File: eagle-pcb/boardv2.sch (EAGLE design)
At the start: 11 parts, among them IC1 ATTINY85, J1 FEMALE 2x3, X1 USBPCB

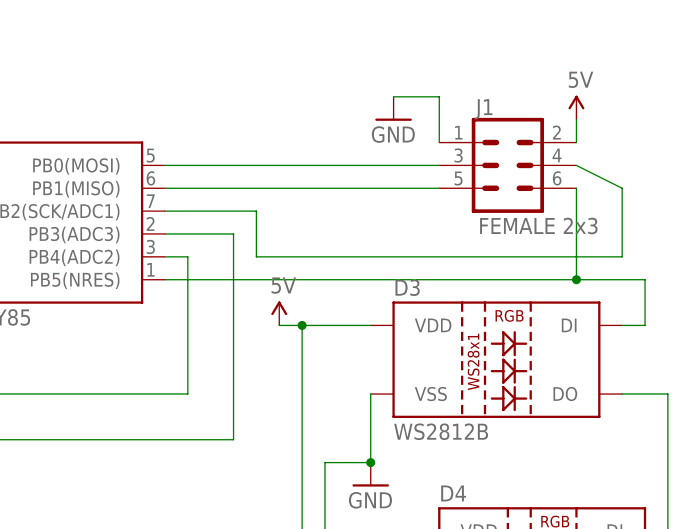
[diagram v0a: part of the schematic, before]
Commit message: FIX pcb, use MOSI to drive LED, not RESET
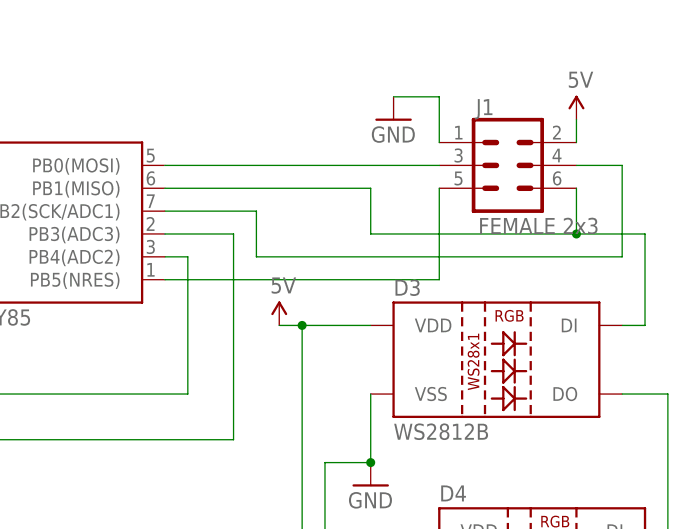
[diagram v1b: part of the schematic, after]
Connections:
- removed net RESET/LED: D3.DI, IC1.PB5(NRES), J1.6
- new net RESET: IC1.PB5(NRES), J1.5
- net MISO: now also D3.DI, J1.6; no longer J1.5
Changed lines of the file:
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@@
 <?xml version="1.0" encoding="utf-8"?>
 <!DOCTYPE eagle SYSTEM "eagle.dtd">
-<eagle version="9.6.1">
+<eagle version="9.6.2">
 <drawing>
 <settings>
@@
 </segment>
 </net>
-<net name="RESET/LED" class="0">
-<segment>
-<pinref part="D3" gate="G$1" pin="DI"/>
-<wire x1="127" y1="27.94" x2="124.46" y2="27.94" width="0.1524" layer="91"/>
-<wire x1="127" y1="33.02" x2="127" y2="27.94" width="0.1524" layer="91"/>
+<net name="RESET" class="0">
+<segment>
 <pinref part="IC1" gate="G$1" pin="PB5(NRES)"/>
-<wire x1="73.66" y1="33.02" x2="119.38" y2="33.02" width="0.1524" layer="91"/>
-<pinref part="J1" gate="G$1" pin="6"/>
-<wire x1="119.38" y1="33.02" x2="127" y2="33.02" width="0.1524" layer="91"/>
-<wire x1="119.38" y1="43.18" x2="119.38" y2="33.02" width="0.1524" layer="91"/>
-<junction x="119.38" y="33.02"/>
+<wire x1="73.66" y1="33.02" x2="104.14" y2="33.02" width="0.1524" layer="91"/>
+<pinref part="J1" gate="G$1" pin="5"/>
+<wire x1="104.14" y1="43.18" x2="104.14" y2="33.02" width="0.1524" layer="91"/>
 </segment>
 </net>
@@
 <wire x1="83.82" y1="35.56" x2="124.46" y2="35.56" width="0.1524" layer="91"/>
 <pinref part="J1" gate="G$1" pin="4"/>
-<wire x1="124.46" y1="35.56" x2="124.46" y2="43.18" width="0.1524" layer="91"/>
-<wire x1="124.46" y1="43.18" x2="119.38" y2="45.72" width="0.1524" layer="91"/>
+<wire x1="124.46" y1="35.56" x2="124.46" y2="45.72" width="0.1524" layer="91"/>
+<wire x1="124.46" y1="45.72" x2="119.38" y2="45.72" width="0.1524" layer="91"/>
 </segment>
 </net>
@@
 <segment>
 <pinref part="IC1" gate="G$1" pin="PB1(MISO)"/>
-<pinref part="J1" gate="G$1" pin="5"/>
-<wire x1="73.66" y1="43.18" x2="104.14" y2="43.18" width="0.1524" layer="91"/>
-</segment>
-</net>
+<wire x1="73.66" y1="43.18" x2="96.52" y2="43.18" width="0.1524" layer="91"/>
+<wire x1="96.52" y1="43.18" x2="96.52" y2="38.1" width="0.1524" layer="91"/>
+<wire x1="96.52" y1="38.1" x2="119.38" y2="38.1" width="0.1524" layer="91"/>
+<pinref part="D3" gate="G$1" pin="DI"/>
+<wire x1="119.38" y1="38.1" x2="127" y2="38.1" width="0.1524" layer="91"/>
+<wire x1="127" y1="27.94" x2="124.46" y2="27.94" width="0.1524" layer="91"/>
+<wire x1="127" y1="38.1" x2="127" y2="27.94" width="0.1524" layer="91"/>
+<pinref part="J1" gate="G$1" pin="6"/>
+<wire x1="119.38" y1="43.18" x2="119.38" y2="38.1" width="0.1524" layer="91"/>
+<junction x="119.38" y="38.1"/>
+</segment>
+</net>
